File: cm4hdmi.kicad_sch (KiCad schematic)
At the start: 8 parts, among them J2 2086581051, U3 AP22653FDZ-7, U4 TPD8S009DSMR

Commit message: respin
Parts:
- renumbered C5 to C7, C6 to C8, C7 to C9, R13 to R16, R14 to R17, U3 to U4, U4 to U5
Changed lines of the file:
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@@
   (symbol (lib_id "Power_Protection_Diodes:AP22653FDZ-7") (at 86.36 153.67 0) (unit 1)
     (in_bom yes) (on_board yes)
-    (property "Reference" "U3" (id 0) (at 86.36 144.78 0))
+    (property "Reference" "U4" (id 0) (at 86.36 144.78 0))
     (property "Value" "AP22653FDZ-7" (id 1) (at 86.36 147.32 0))
     (property "Footprint" "Power_Protection_Diodes:Diodes_W-DFN2020-6_A1" (id 2) (at 86.36 167.64 0)
@@
   (symbol (lib_id "Device:R_Small") (at 105.41 153.67 90) (unit 1)
     (in_bom yes) (on_board yes)
-    (property "Reference" "R14" (id 0) (at 107.95 156.21 90)
+    (property "Reference" "R17" (id 0) (at 107.95 156.21 90)
       (effects (font (size 1.27 1.27)) (justify left))
     )
@@
   (symbol (lib_id "Power_Protection_TI:TPD8S009DSMR") (at 227.33 69.85 90) (mirror x) (unit 1)
     (in_bom yes) (on_board yes)
-    (property "Reference" "U4" (id 0) (at 205.74 74.93 90)
+    (property "Reference" "U5" (id 0) (at 205.74 74.93 90)
       (effects (font (size 1.524 1.524)) (justify right))
     )
@@
   (symbol (lib_id "Device:R_Small") (at 86.36 160.02 270) (unit 1)
     (in_bom yes) (on_board yes)
-    (property "Reference" "R13" (id 0) (at 86.36 162.56 90))
+    (property "Reference" "R16" (id 0) (at 86.36 162.56 90))
     (property "Value" "10k" (id 1) (at 86.36 165.1 90))
     (property "Footprint" "Resistor_SMD:R_0402_1005Metric" (id 2) (at 86.36 160.02 0)
@@
   (symbol (lib_id "power:GND") (at 104.14 110.49 0) (unit 1)
     (in_bom yes) (on_board yes) (fields_autoplaced)
-    (property "Reference" "#PWR013" (id 0) (at 104.14 116.84 0)
+    (property "Reference" "#PWR014" (id 0) (at 104.14 116.84 0)
       (effects (font (size 1.27 1.27)) hide)
     )
@@
   (symbol (lib_id "power:GND") (at 248.92 63.5 0) (unit 1)
     (in_bom yes) (on_board yes)
-    (property "Reference" "#PWR015" (id 0) (at 248.92 69.85 0)
+    (property "Reference" "#PWR016" (id 0) (at 248.92 69.85 0)
       (effects (font (size 1.27 1.27)) hide)
     )
@@
   (symbol (lib_id "Device:C_Small") (at 137.16 157.48 0) (unit 1)
     (in_bom yes) (on_board yes)
-    (property "Reference" "C7" (id 0) (at 138.43 156.21 0)
+    (property "Reference" "C9" (id 0) (at 138.43 156.21 0)
       (effects (font (size 1.27 1.27)) (justify left))
     )
@@
   (symbol (lib_id "power:GND") (at 137.16 170.18 0) (unit 1)
     (in_bom yes) (on_board yes)
-    (property "Reference" "#PWR014" (id 0) (at 137.16 176.53 0)
+    (property "Reference" "#PWR015" (id 0) (at 137.16 176.53 0)
       (effects (font (size 1.27 1.27)) hide)
     )
@@
   (symbol (lib_id "Device:C_Small") (at 127 157.48 0) (unit 1)
     (in_bom yes) (on_board yes)
-    (property "Reference" "C6" (id 0) (at 128.27 156.21 0)
+    (property "Reference" "C8" (id 0) (at 128.27 156.21 0)
       (effects (font (size 1.27 1.27)) (justify left))
     )
@@
   (symbol (lib_id "Device:C_Small") (at 57.15 156.21 0) (unit 1)
     (in_bom yes) (on_board yes)
-    (property "Reference" "C5" (id 0) (at 58.42 154.94 0)
-      (effects (font (size 1.27 1.27)) (justify left))
-    )
+    (property "Reference" "C7" (id 0) (at 58.42 154.94 0)
+      (effects (font (size 1.27 1.27)) (justify left))
+    )

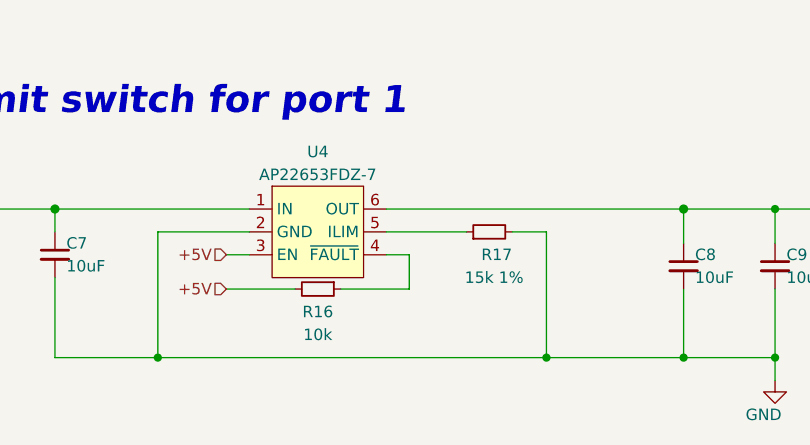
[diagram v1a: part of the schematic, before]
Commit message: fixed I2C ping indicator
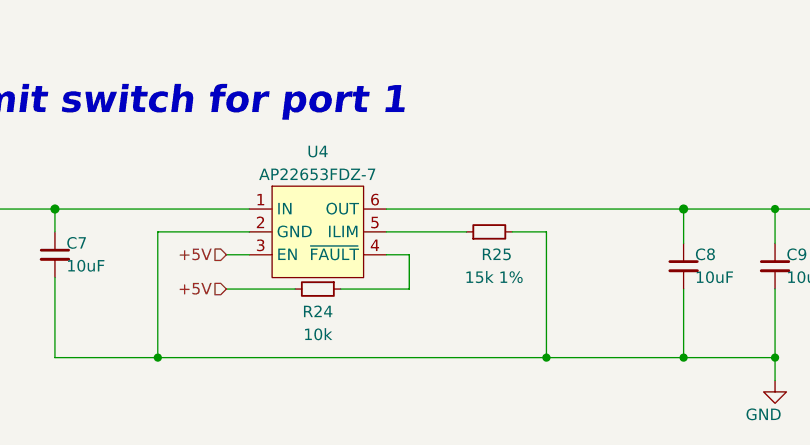
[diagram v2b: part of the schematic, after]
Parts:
- renumbered R16 to R24, R17 to R25
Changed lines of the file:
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@@
   (symbol (lib_id "Device:R_Small") (at 105.41 153.67 90) (unit 1)
     (in_bom yes) (on_board yes)
-    (property "Reference" "R17" (id 0) (at 107.95 156.21 90)
+    (property "Reference" "R25" (id 0) (at 107.95 156.21 90)
       (effects (font (size 1.27 1.27)) (justify left))
     )
@@
   (symbol (lib_id "Device:R_Small") (at 86.36 160.02 270) (unit 1)
     (in_bom yes) (on_board yes)
-    (property "Reference" "R16" (id 0) (at 86.36 162.56 90))
+    (property "Reference" "R24" (id 0) (at 86.36 162.56 90))
     (property "Value" "10k" (id 1) (at 86.36 165.1 90))
     (property "Footprint" "Resistor_SMD:R_0402_1005Metric" (id 2) (at 86.36 160.02 0)
@@
   (symbol (lib_id "power:GND") (at 104.14 110.49 0) (unit 1)
     (in_bom yes) (on_board yes) (fields_autoplaced)
-    (property "Reference" "#PWR014" (id 0) (at 104.14 116.84 0)
+    (property "Reference" "#PWR016" (id 0) (at 104.14 116.84 0)
       (effects (font (size 1.27 1.27)) hide)
     )
@@
   (symbol (lib_id "power:GND") (at 248.92 63.5 0) (unit 1)
     (in_bom yes) (on_board yes)
-    (property "Reference" "#PWR016" (id 0) (at 248.92 69.85 0)
+    (property "Reference" "#PWR018" (id 0) (at 248.92 69.85 0)
       (effects (font (size 1.27 1.27)) hide)
     )
@@
   (symbol (lib_id "power:GND") (at 137.16 170.18 0) (unit 1)
     (in_bom yes) (on_board yes)
-    (property "Reference" "#PWR015" (id 0) (at 137.16 176.53 0)
+    (property "Reference" "#PWR017" (id 0) (at 137.16 176.53 0)
       (effects (font (size 1.27 1.27)) hide)
     )

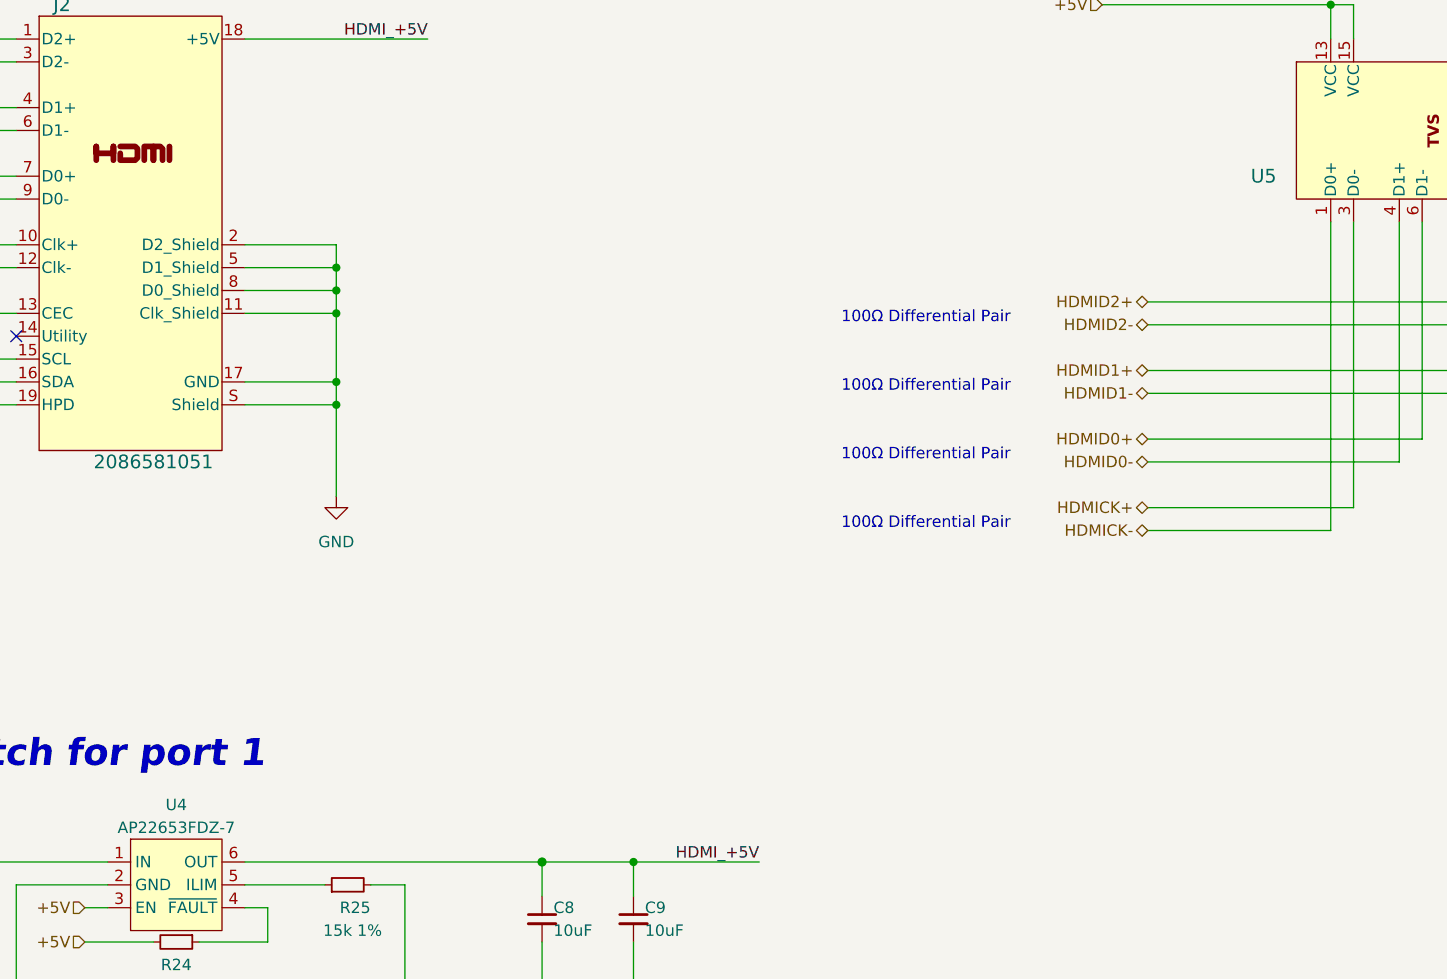
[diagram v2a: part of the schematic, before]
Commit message: added ti buffer lib
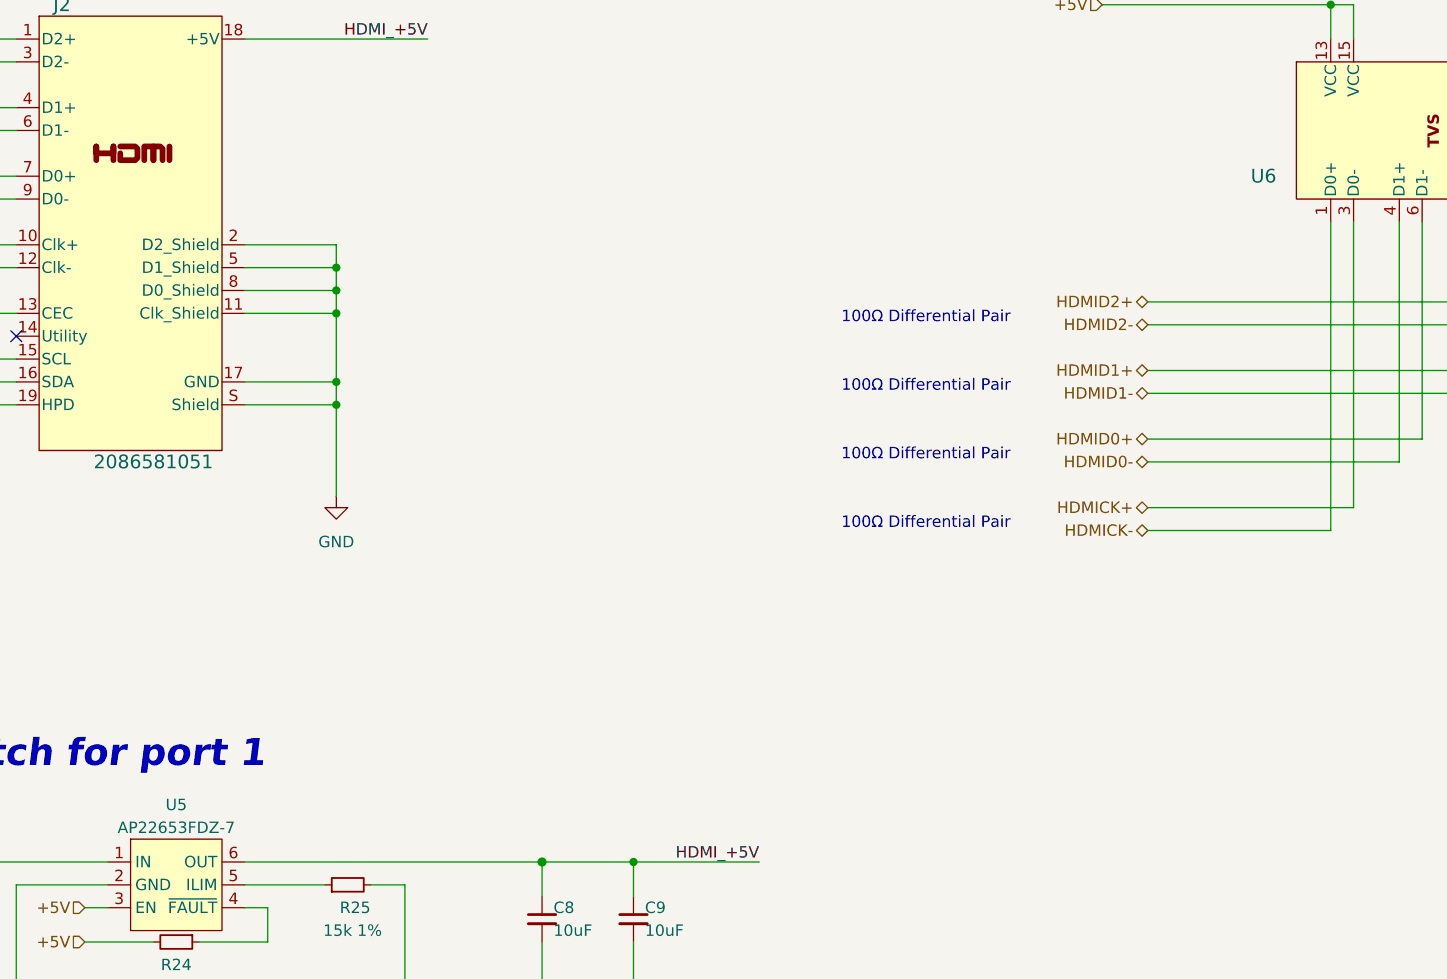
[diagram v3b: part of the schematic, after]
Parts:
- renumbered U4 to U5, U5 to U6
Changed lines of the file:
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@@
   (symbol (lib_id "Power_Protection_Diodes:AP22653FDZ-7") (at 86.36 153.67 0) (unit 1)
     (in_bom yes) (on_board yes)
-    (property "Reference" "U4" (id 0) (at 86.36 144.78 0))
+    (property "Reference" "U5" (id 0) (at 86.36 144.78 0))
     (property "Value" "AP22653FDZ-7" (id 1) (at 86.36 147.32 0))
     (property "Footprint" "Power_Protection_Diodes:Diodes_W-DFN2020-6_A1" (id 2) (at 86.36 167.64 0)
@@
   (symbol (lib_id "Power_Protection_TI:TPD8S009DSMR") (at 227.33 69.85 90) (mirror x) (unit 1)
     (in_bom yes) (on_board yes)
-    (property "Reference" "U5" (id 0) (at 205.74 74.93 90)
+    (property "Reference" "U6" (id 0) (at 205.74 74.93 90)
       (effects (font (size 1.524 1.524)) (justify right))
     )
@@
   (symbol (lib_id "power:GND") (at 104.14 110.49 0) (unit 1)
     (in_bom yes) (on_board yes) (fields_autoplaced)
-    (property "Reference" "#PWR016" (id 0) (at 104.14 116.84 0)
+    (property "Reference" "#PWR018" (id 0) (at 104.14 116.84 0)
       (effects (font (size 1.27 1.27)) hide)
     )
@@
   (symbol (lib_id "power:GND") (at 248.92 63.5 0) (unit 1)
     (in_bom yes) (on_board yes)
-    (property "Reference" "#PWR018" (id 0) (at 248.92 69.85 0)
+    (property "Reference" "#PWR020" (id 0) (at 248.92 69.85 0)
       (effects (font (size 1.27 1.27)) hide)
     )
@@
   (symbol (lib_id "power:GND") (at 137.16 170.18 0) (unit 1)
     (in_bom yes) (on_board yes)
-    (property "Reference" "#PWR017" (id 0) (at 137.16 176.53 0)
-      (effects (font (size 1.27 1.27)) hide)
-    )
+    (property "Reference" "#PWR019" (id 0) (at 137.16 176.53 0)
+      (effects (font (size 1.27 1.27)) hide)
+    )
